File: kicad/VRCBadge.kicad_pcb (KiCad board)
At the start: 2 copper layers, 34 parts, among them J4 Conn_01x02, J5 USB_C_Receptacle_USB2.0_16P, J6 Conn_01x13_Socket, Q2 FS8205A, SW3 RESET, SW4 BOOT, U10 MAX17048G+T10, U6 DW01A, U7 ME6211C33M5, U8 TP4056-42-ESOP8, U9 ESP32-S3-WROOM-1U

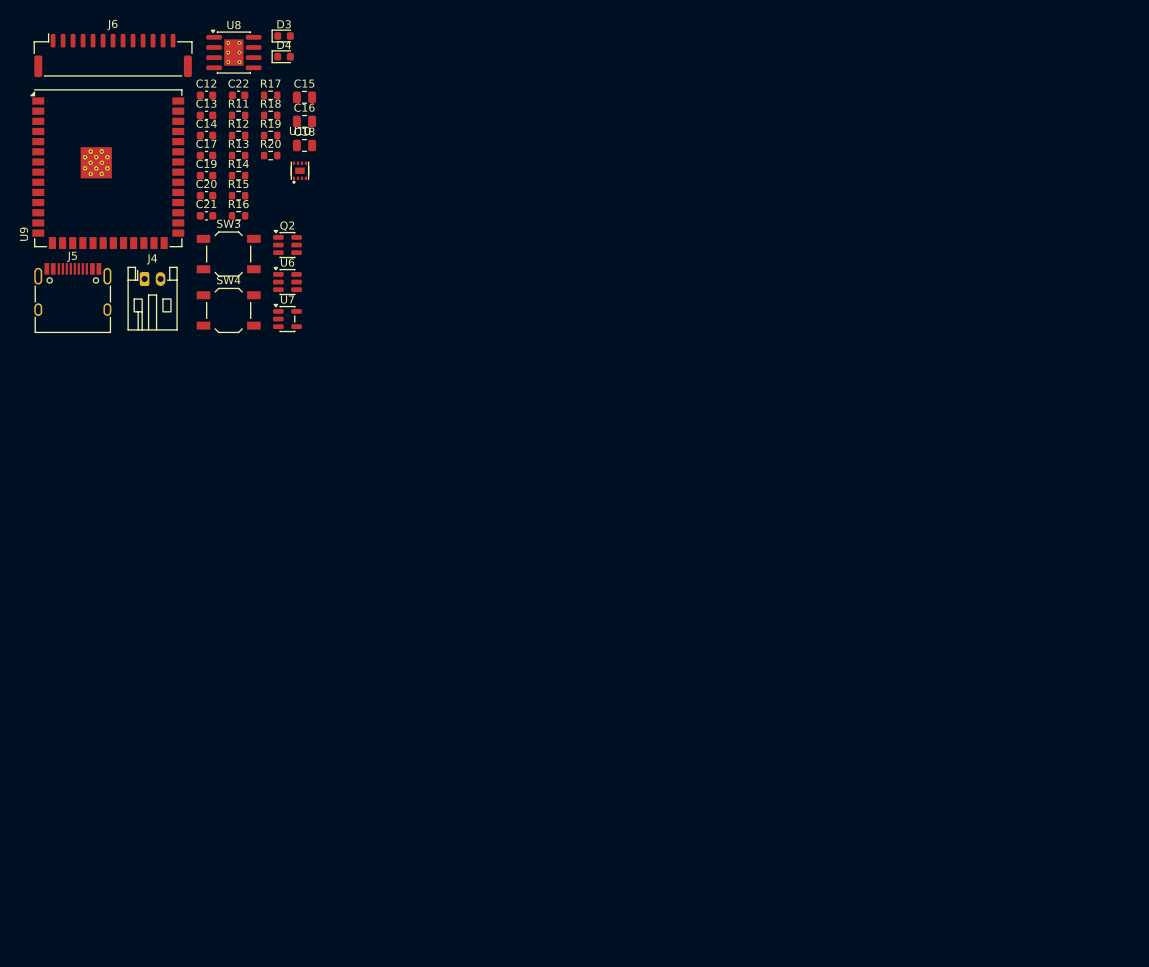
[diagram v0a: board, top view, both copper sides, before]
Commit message: feat: add board outline and initial component placement
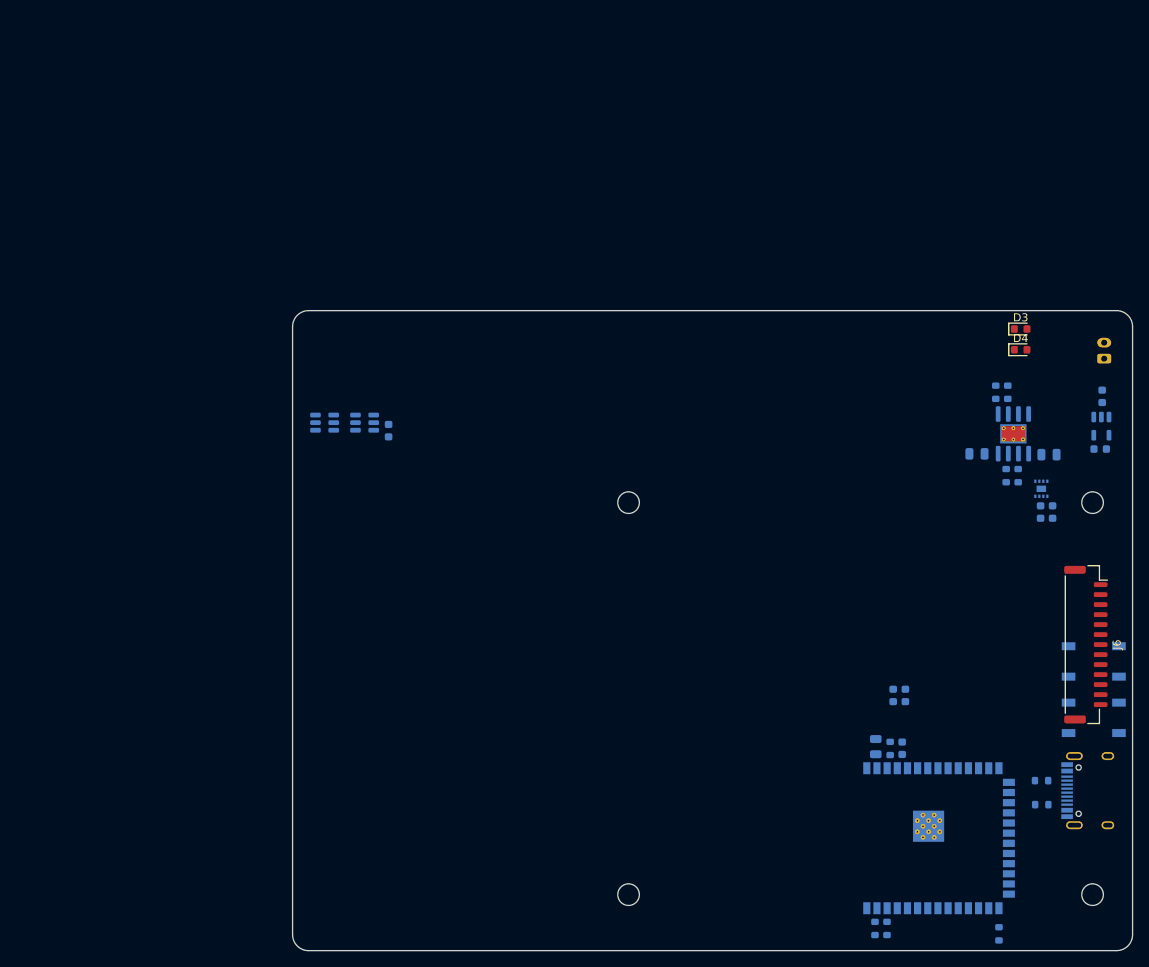
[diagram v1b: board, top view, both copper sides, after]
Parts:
- added REF**: MountingHole_2.7mm_M2.5, MountingHole:MountingHole_2.7mm_M2.5, F.Cu at (100.0, 73.0)
- added REF**: MountingHole_2.7mm_M2.5, MountingHole:MountingHole_2.7mm_M2.5, F.Cu at (42.0, 73.0)
- added REF**: MountingHole_2.7mm_M2.5, MountingHole:MountingHole_2.7mm_M2.5, F.Cu at (42.0, 24.0)
- added REF**: MountingHole_2.7mm_M2.5, MountingHole:MountingHole_2.7mm_M2.5, F.Cu at (100.0, 24.0)
- C12, C13, C14, C15, C16, C17, C18, C19, C20, C21, C22, J4, Q2, R11, R12, R13, R14, R15, R16, R17, R18, R19, R20, SW3, SW4, U10, U6, U7, U8, U9: moved to B.Cu
- J5: value USB_C_Receptacle_USB2.0_16P -> USB_C; moved to B.Cu
- moved J5 142.2 mm to (100.9, 60.0), turned to -90 degrees
- moved J6 142.2 mm to (99.2, 41.8), turned to -90 degrees
- moved R18 136.9 mm to (88.3, 77.9), turned to 90 degrees
- moved U9 132.9 mm to (80.2, 66.0), turned to -90 degrees
- moved R11 132.3 mm to (93.7, 61.8), turned to 180 degrees
- moved R12 128.8 mm to (93.6, 58.8), turned to 180 degrees
- moved R19 124.6 mm to (72.8, 77.2), turned to 90 degrees
- moved R20 123.6 mm to (74.3, 77.2), turned to 90 degrees
- moved J4 120.4 mm to (101.5, 6.00), turned to 90 degrees
- moved SW3 119.5 mm to (100.2, 43.9)
- moved SW4 119.5 mm to (100.2, 50.9)
- moved C14 118.4 mm to (101.0, 17.3)
- moved C13 117.3 mm to (101.2, 10.7), turned to 90 degrees
- moved C17 114.2 mm to (76.2, 54.7), turned to 90 degrees
- moved C22 113.0 mm to (93.5, 25.2), turned to -90 degrees
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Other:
- board outline added: 105 x 80 mm

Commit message: wip: pcb
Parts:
- removed REF** (x4): MountingHole_2.7mm_M2.5, MountingHole:MountingHole_2.7mm_M2.5
- C12, C13, C14, C17, C19, C20, C21, C22: footprint Capacitor_SMD:C_0603_1608Metric -> Capacitor_SMD:C_0402_1005Metric
- C15, C16, C18: footprint Capacitor_SMD:C_0805_2012Metric -> Capacitor_SMD:C_0402_1005Metric
- D3, D4: footprint LED_SMD:LED_0603_1608Metric -> LED_SMD:LED_0402_1005Metric; moved to B.Cu
- J5: value USB_C -> USB_C_Receptacle_USB2.0_16P
- R11, R12, R13, R14, R15, R16, R17, R18, R19, R20: footprint Resistor_SMD:R_0603_1608Metric -> Resistor_SMD:R_0402_1005Metric
- moved J4 101.7 mm to (4.00, 35.0), turned to -90 degrees
- moved C16 97.9 mm to (1.24, 47.5), turned to 90 degrees
- moved R15 97.5 mm to (3.77, 56.9), turned to 90 degrees
- moved J5 96.8 mm to (4.15, 63.2), turned to 90 degrees
- moved R16 95.1 mm to (5.07, 56.9), turned to 90 degrees
- moved U8 94.4 mm to (3.14, 52.2), turned to 90 degrees
- moved C13 93.2 mm to (10.3, 31.4), turned to -90 degrees
- moved C15 92.9 mm to (1.24, 56.8), turned to -90 degrees
- moved U7 92.8 mm to (9.34, 28.3), turned to 90 degrees
- moved D3 91.5 mm to (8.20, 41.2), turned to 90 degrees
- moved C14 91.0 mm to (10.3, 25.3), turned to 90 degrees
- moved D4 89.3 mm to (9.47, 41.2), turned to 90 degrees
- moved R14 84.3 mm to (9.47, 43.1)
- moved R13 84.1 mm to (8.20, 43.1)
- moved R12 83.4 mm to (10.4, 64.4), turned to 0 degrees
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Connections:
- net USB_DN renamed D-
- net USB_DP renamed D+
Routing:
- net VBUS: track 0.00 -> 26.2 mm, vias 0 -> 4
- net OC: track 0.00 -> 16.4 mm
- net CS: track 0.00 -> 15.2 mm
- net OD: track 0.00 -> 12.0 mm
- net +BATT: track 0.00 -> 10.1 mm, vias 0 -> 2
- net D+: track 0.00 -> 7.84 mm
- net D-: track 0.00 -> 7.84 mm
- net -BATT: track 0.00 -> 7.78 mm, vias 0 -> 1
- net Net-(J5-CC2): track 0.00 -> 1.70 mm
- net Net-(J5-CC1): track 0.00 -> 1.70 mm
- net +3V3: track 0.00 -> 1.37 mm
- added copper zone on In1.Cu, net +BATT
- added copper zone on In2.Cu, net GND
- added copper zone on In1.Cu, net VBUS
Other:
- board size 105 x 80 mm -> 102 x 80 mm
- copper layers 2 -> 4
